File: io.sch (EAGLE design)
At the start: 34 parts, among them J1 SJ-3502-SMT-TR, Q1 MMBT2222A, Q2 2SCR574D3TL1, U1 MCP1703T-5002E, U3 LM386M-1, X1 Antenna

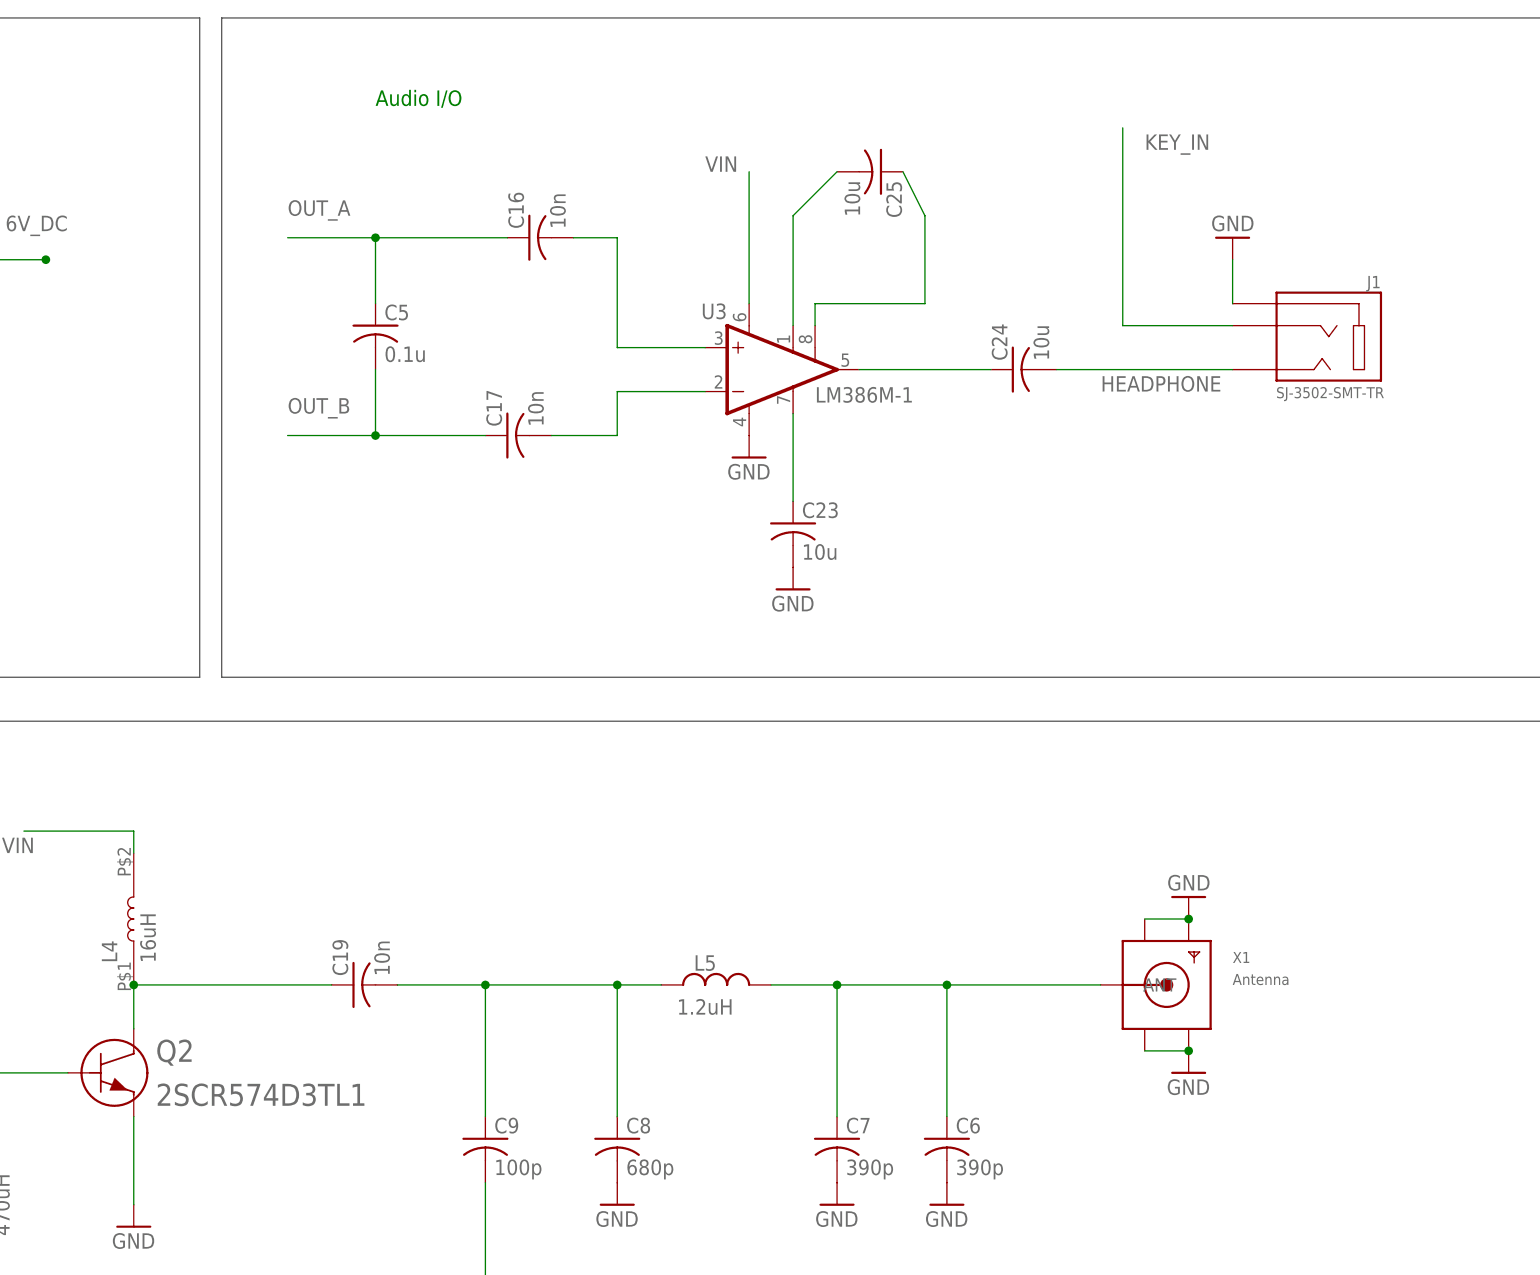
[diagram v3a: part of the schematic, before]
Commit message: Updated boarts to v1.1
9VuTX Version 1.1

Several adjustments after mockup with V 1.0 of the board. That first version would be non-functional due to a few layout mismatches.

* fixed 2nd transistor layout to actually match part / spec (TO-252)
* rotated potentiometers 180 degrees so they face outward instead toward the middle of the board
* expanded pads of L2 (450uH inductor) to match recommended spec
* replaced phone jack with a true surface mount version (SJ-3523-SMT-TR)
* re-arranged the IO board to allow for the different phone jack
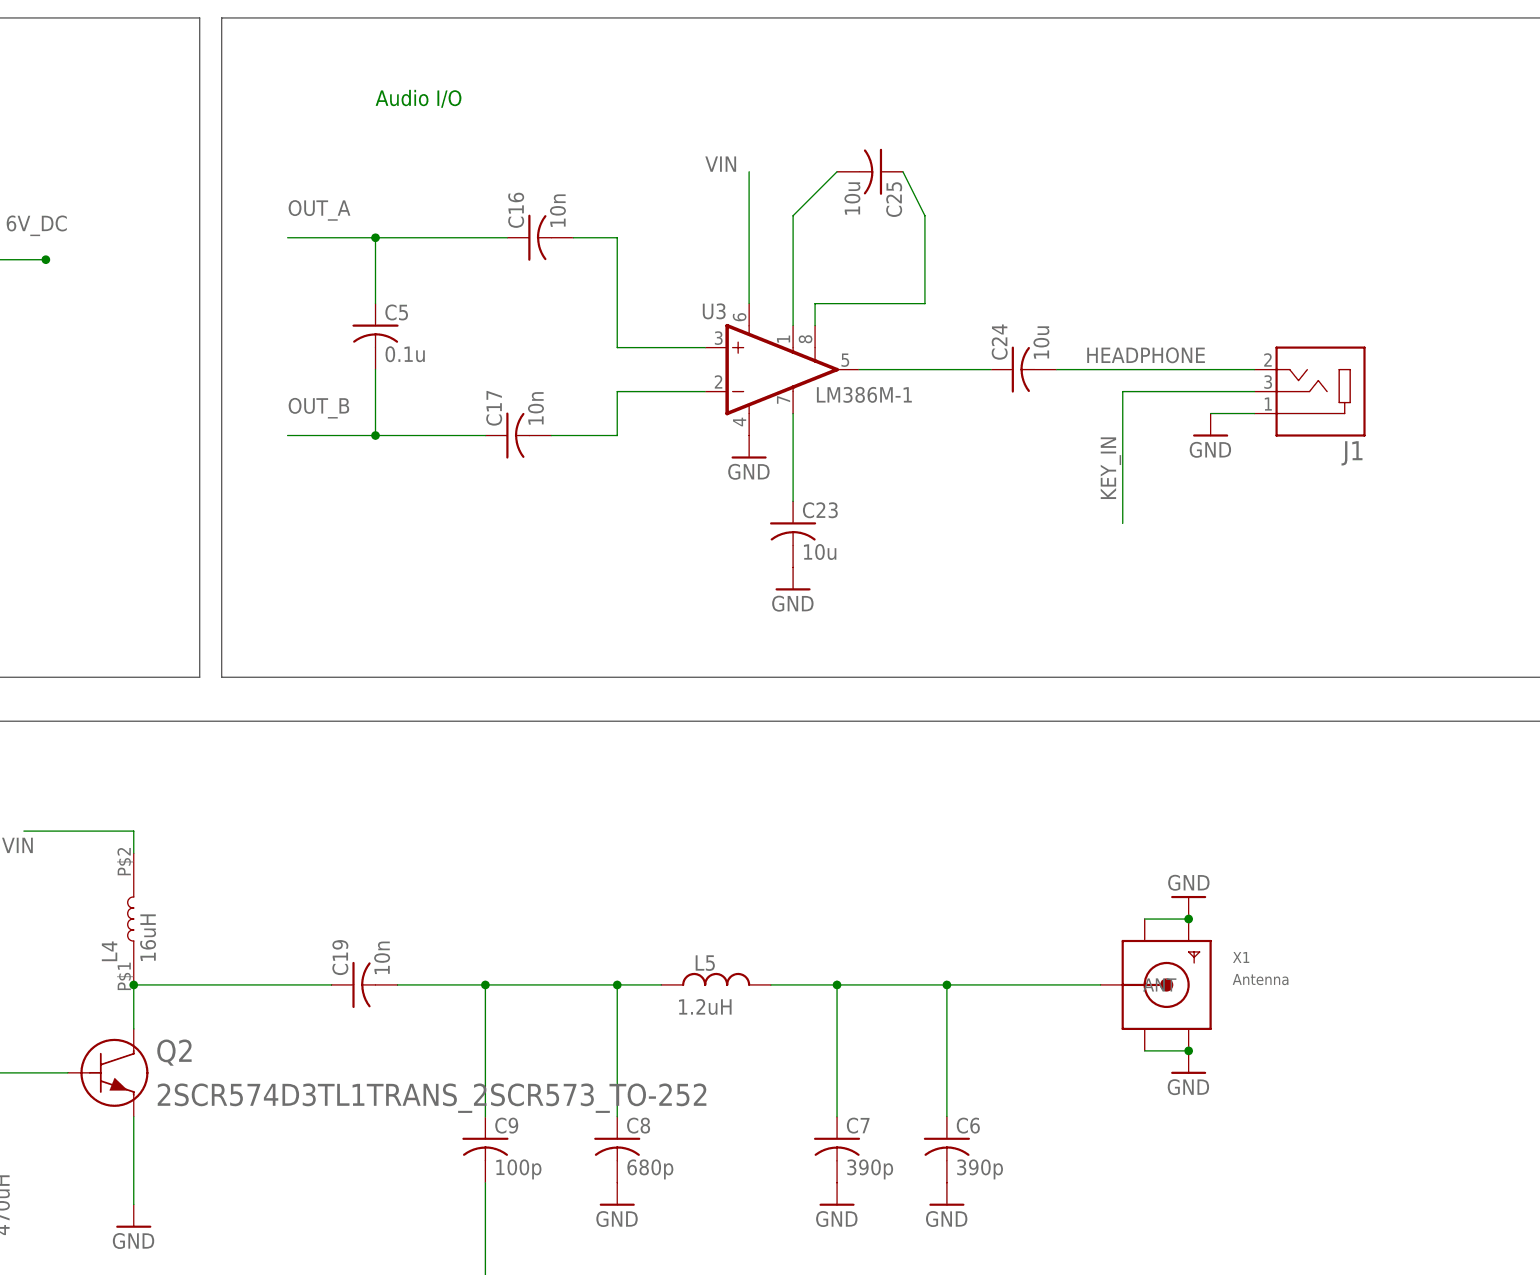
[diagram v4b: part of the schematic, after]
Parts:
- J1: value SJ-3502-SMT-TR -> SJ-3523-SMT-TR; device Audio Connectors:SJ-3502-SMT-TR -> SJ-3523-SMT-TR:SJ-3523-SMT-TR
- L2: device Inductor:L_CHIP-1008(2520-METRIC) -> zort2:L_CHIP-1008(2520-METRIC)
- Q2: value 2SCR574D3TL1 -> 2SCR574D3TL1TRANS_2SCR573_TO-252; device zort2:2SCR574D3TL1 -> zort2:2SCR574D3TL1TRANS_2SCR573_TO-252
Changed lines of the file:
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@@
 <part name="GND8" library="supply1" library_urn="urn:adsk.eagle:library:371" deviceset="GND" device=""/>
 <part name="GND9" library="supply1" library_urn="urn:adsk.eagle:library:371" deviceset="GND" device=""/>
-<part name="J1" library="Audio Connectors" library_urn="urn:adsk.eagle:library:16251796" deviceset="SJ-3502-SMT-TR" device="" package3d_urn="urn:adsk.eagle:package:16225242/5"/>
 <part name="GND10" library="supply1" library_urn="urn:adsk.eagle:library:371" deviceset="GND" device=""/>
 <part name="C12" library="adafruit" library_urn="urn:adsk.eagle:library:420" deviceset="C-US" device="C0805" package3d_urn="urn:adsk.eagle:package:6240337/1" value="150p"/>
@@
 <part name="L5" library="Inductor" library_urn="urn:adsk.eagle:library:16378440" deviceset="L" device="CHIP-0805(2012-METRIC)" package3d_urn="urn:adsk.eagle:package:16378480/1" technology="_" value="1.2uH"/>
 <part name="L4" library="zort2" deviceset="B966AS-160M-P3" device="" value="16uH"/>
-<part name="L2" library="Inductor" library_urn="urn:adsk.eagle:library:16378440" deviceset="L" device="CHIP-1008(2520-METRIC)" package3d_urn="urn:adsk.eagle:package:16378469/1" technology="_" value="470uH"/>
-<part name="Q2" library="zort2" deviceset="2SCR574D3TL1" device=""/>
 <part name="Q1" library="zort2" deviceset="MMBT2222A-7-F" device="SOT-23_DIO-M" value="MMBT2222A"/>
 <part name="U$1" library="zort2" deviceset="9V_968" device="9V_968_SMD"/>
+<part name="Q2" library="zort2" deviceset="2SCR574D3TL1" device="TRANS_2SCR573_TO-252"/>
+<part name="L2" library="zort2" deviceset="L" device="CHIP-1008(2520-METRIC)" package3d_urn="urn:adsk.eagle:package:16378469/1" technology="_" value="470uH"/>
+<part name="J1" library="SJ-3523-SMT-TR" deviceset="SJ-3523-SMT-TR" device=""/>
 </parts>
 <sheets>
@@
 <attribute name="VALUE" x="116.84" y="53.34" size="1.778" layer="96"/>
 </instance>
-<instance part="J1" gate="G$1" x="182.88" y="83.82" smashed="yes" rot="MR0">
-<attribute name="VALUE" x="187.706" y="77.978" size="1.27035" layer="96" rot="MR0"/>
-<attribute name="NAME" x="187.32991875" y="90.68325" size="1.4224" layer="95" rot="MR0"/>
-</instance>
-<instance part="GND10" gate="1" x="170.18" y="96.52" smashed="yes" rot="R180">
-<attribute name="VALUE" x="172.72" y="99.06" size="1.778" layer="96" rot="R180"/>
+<instance part="GND10" gate="1" x="167.64" y="73.66" smashed="yes">
+<attribute name="VALUE" x="165.1" y="71.12" size="1.778" layer="96"/>
 </instance>
 <instance part="C12" gate="G$1" x="-73.66" y="17.78" smashed="yes">
@@
 <attribute name="VALUE" x="45.72271875" y="12.694559375" size="1.779909375" layer="96" rot="R90"/>
 </instance>
+<instance part="Q1" gate="A" x="-60.96" y="-20.32" smashed="yes">
+<attribute name="NAME" x="-50.4444" y="-13.7414" size="2.0828" layer="95" ratio="6" rot="SR0"/>
+<attribute name="VALUE" x="-51.0794" y="-26.4414" size="2.0828" layer="96" ratio="6" rot="SR0"/>
+</instance>
+<instance part="U$1" gate="G$1" x="-78.74" y="88.9" smashed="yes"/>
+<instance part="Q2" gate="A" x="40.64" y="0" smashed="yes">
+<attribute name="NAME" x="45.72" y="1.27" size="2.54" layer="95" ratio="10" rot="SR0"/>
+<attribute name="VALUE" x="45.72" y="-3.81" size="2.54" layer="96" ratio="10" rot="SR0"/>
+</instance>
 <instance part="L2" gate="G$1" x="25.4" y="-15.24" smashed="yes" rot="R90">
 <attribute name="NAME" x="22.86" y="-15.24" size="1.778" layer="95" rot="R90" align="center"/>
 <attribute name="VALUE" x="27.94" y="-15.24" size="1.778" layer="96" rot="R90" align="center"/>
 </instance>
-<instance part="Q2" gate="A" x="40.64" y="0" smashed="yes">
-<attribute name="NAME" x="45.72" y="1.27" size="2.54" layer="95" ratio="10" rot="SR0"/>
-<attribute name="VALUE" x="45.72" y="-3.81" size="2.54" layer="96" ratio="10" rot="SR0"/>
-</instance>
-<instance part="Q1" gate="A" x="-60.96" y="-20.32" smashed="yes">
-<attribute name="NAME" x="-50.4444" y="-13.7414" size="2.0828" layer="95" ratio="6" rot="SR0"/>
-<attribute name="VALUE" x="-51.0794" y="-26.4414" size="2.0828" layer="96" ratio="6" rot="SR0"/>
-</instance>
-<instance part="U$1" gate="G$1" x="-78.74" y="88.9" smashed="yes"/>
+<instance part="J1" gate="G$1" x="180.34" y="78.74" smashed="yes" rot="R180">
+<attribute name="NAME" x="185.440409375" y="73.002040625" size="2.201440625" layer="95" rot="R180"/>
+</instance>
 </instances>
 <busses>
@@
 </segment>
 <segment>
+<pinref part="GND10" gate="1" pin="GND"/>
+<wire x1="167.64" y1="76.2" x2="172.72" y2="76.2" width="0.1524" layer="91"/>
 <pinref part="J1" gate="G$1" pin="1"/>
-<pinref part="GND10" gate="1" pin="GND"/>
-<wire x1="170.18" y1="93.98" x2="170.18" y2="88.9" width="0.1524" layer="91"/>
 </segment>
 <segment>
@@
 </segment>
 <segment>
+<pinref part="GND1" gate="1" pin="GND"/>
+<pinref part="U$1" gate="G$1" pin="P$2"/>
+</segment>
+<segment>
 <pinref part="GND21" gate="1" pin="GND"/>
 <pinref part="L2" gate="G$1" pin="1"/>
-</segment>
-<segment>
-<pinref part="GND1" gate="1" pin="GND"/>
-<pinref part="U$1" gate="G$1" pin="P$2"/>
 </segment>
 </net>
@@
 <segment>
 <pinref part="C24" gate="G$1" pin="2"/>
+<wire x1="149.86" y1="81.28" x2="172.72" y2="81.28" width="0.1524" layer="91"/>
+<label x="153.162" y="82.042" size="1.778" layer="95"/>
 <pinref part="J1" gate="G$1" pin="2"/>
-<wire x1="149.86" y1="81.28" x2="170.18" y2="81.28" width="0.1524" layer="91"/>
-<label x="154.94" y="78.74" size="1.778" layer="95"/>
 </segment>
 </net>
 <net name="KEY_IN" class="0">
 <segment>
+<label x="154.94" y="73.66" size="1.778" layer="95" rot="R270"/>
 <pinref part="J1" gate="G$1" pin="3"/>
-<wire x1="170.18" y1="86.36" x2="157.48" y2="86.36" width="0.1524" layer="91"/>
-<wire x1="157.48" y1="86.36" x2="157.48" y2="109.22" width="0.1524" layer="91"/>
-<label x="160.02" y="106.68" size="1.778" layer="95"/>
+<wire x1="172.72" y1="78.74" x2="157.48" y2="78.74" width="0.1524" layer="91"/>
+<wire x1="157.48" y1="78.74" x2="157.48" y2="63.5" width="0.1524" layer="91"/>
 </segment>
 <segment>
@@
 </segment>
 </net>
-<net name="N$23" class="0">
+<net name="N$23" class="1">
 <segment>
 <pinref part="R7" gate="G$1" pin="2"/>
@@
 <wire x1="25.4" y1="0" x2="35.56" y2="0" width="0.1524" layer="91"/>
 <junction x="25.4" y="0"/>
+<pinref part="Q2" gate="A" pin="1"/>
 <pinref part="L2" gate="G$1" pin="2"/>
-<pinref part="Q2" gate="A" pin="1"/>
-</segment>
-</net>
-<net name="N$24" class="0">
+</segment>
+</net>
+<net name="N$24" class="1">
 <segment>
 <wire x1="43.18" y1="5.08" x2="43.18" y2="10.16" width="0.1524" layer="91"/>
@@
 </segment>
 </net>
-<net name="N$25" class="0">
+<net name="N$25" class="1">
 <segment>
 <pinref part="C19" gate="G$1" pin="2"/>
@@
 </segment>
 </net>
-<net name="N$26" class="0">
+<net name="N$26" class="1">
 <segment>
 <wire x1="116.84" y1="10.16" x2="124.46" y2="10.16" width="0.1524" layer="91"/>

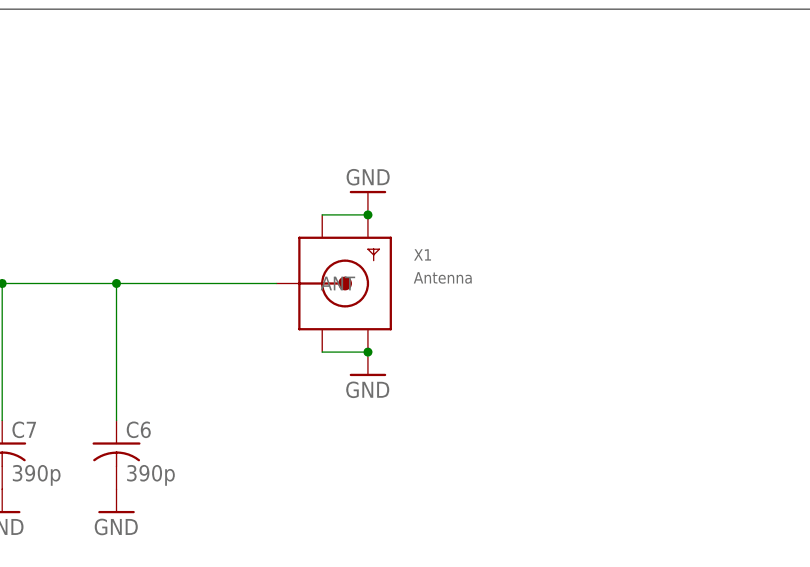
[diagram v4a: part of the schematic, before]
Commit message: continuing on v 1.1
* removed "label" label from SMA connector
* increased the width of some lines likely to carry higher current
* attempted to clean up some little stuff
* updated images
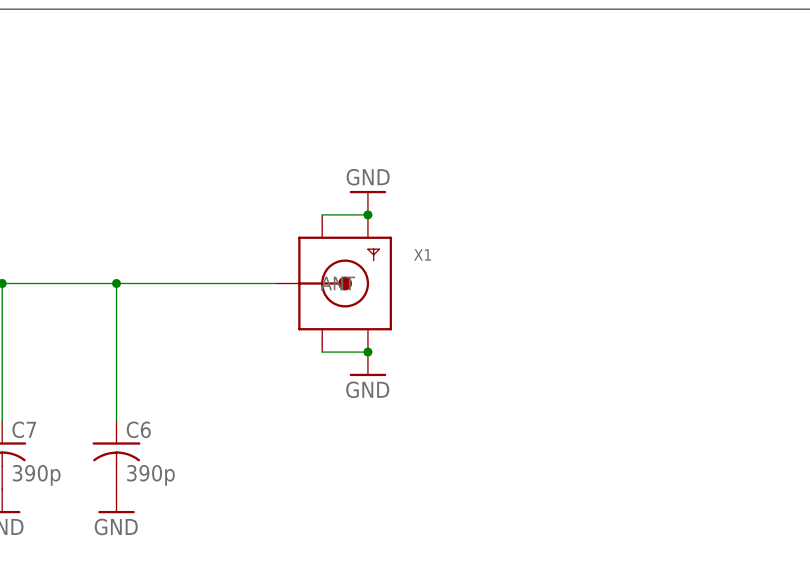
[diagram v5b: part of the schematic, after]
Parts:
- X1: value Antenna -> (none); device adafruit:SMACONNECTOR_EDGE -> zort2:SMACONNECTOR_EDGE
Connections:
- new net N$1: X1.GND3
- new net N$2: X1.GND1
- net GND: no longer X1.GND1, X1.GND3
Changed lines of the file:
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@@
 <part name="GND19" library="supply1" library_urn="urn:adsk.eagle:library:371" deviceset="GND" device=""/>
 <part name="GND20" library="supply1" library_urn="urn:adsk.eagle:library:371" deviceset="GND" device=""/>
-<part name="X1" library="adafruit" library_urn="urn:adsk.eagle:library:420" deviceset="SMACONNECTOR" device="_EDGE" package3d_urn="urn:adsk.eagle:package:6240945/1" value="Antenna"/>
 <part name="L3" library="MLF2012E5R6KT000" deviceset="MLF2012E5R6KT000" device="" value="5.6uH"/>
 <part name="R7" library="adafruit" library_urn="urn:adsk.eagle:library:420" deviceset="R-US_" device="M0805" package3d_urn="urn:adsk.eagle:package:6240587/1" value="100"/>
@@
 <part name="L2" library="zort2" deviceset="L" device="CHIP-1008(2520-METRIC)" package3d_urn="urn:adsk.eagle:package:16378469/1" technology="_" value="470uH"/>
 <part name="J1" library="SJ-3523-SMT-TR" deviceset="SJ-3523-SMT-TR" device=""/>
+<part name="X1" library="zort2" deviceset="SMACONNECTOR" device="_EDGE" package3d_urn="urn:adsk.eagle:package:6240945/1"/>
 </parts>
 <sheets>
@@
 <attribute name="VALUE" x="134.62" y="-17.78" size="1.778" layer="96"/>
 </instance>
-<instance part="X1" gate="G$1" x="162.56" y="10.16" smashed="yes">
-<attribute name="NAME" x="170.18" y="12.7" size="1.27" layer="95"/>
-<attribute name="VALUE" x="170.18" y="10.16" size="1.27" layer="95"/>
-</instance>
 <instance part="L3" gate="G$1" x="-17.78" y="7.62" smashed="yes" rot="R90">
 <attribute name="NAME" x="-19.68818125" y="2.53153125" size="1.780959375" layer="95" rot="R90"/>
@@
 <instance part="J1" gate="G$1" x="180.34" y="78.74" smashed="yes" rot="R180">
 <attribute name="NAME" x="185.440409375" y="73.002040625" size="2.201440625" layer="95" rot="R180"/>
+</instance>
+<instance part="X1" gate="G$1" x="162.56" y="10.16" smashed="yes">
+<attribute name="NAME" x="170.18" y="12.7" size="1.27" layer="95"/>
+<attribute name="VALUE" x="170.18" y="10.16" size="1.27" layer="95"/>
 </instance>
 </instances>
@@
 </segment>
 <segment>
+<pinref part="GND23" gate="1" pin="GND"/>
 <pinref part="X1" gate="G$1" pin="GND4"/>
-<pinref part="GND23" gate="1" pin="GND"/>
-<pinref part="X1" gate="G$1" pin="GND3"/>
-<wire x1="160.02" y1="2.54" x2="165.1" y2="2.54" width="0.1524" layer="91"/>
 <junction x="165.1" y="2.54"/>
 </segment>
 <segment>
-<pinref part="X1" gate="G$1" pin="GND1"/>
+<pinref part="GND24" gate="1" pin="GND"/>
 <pinref part="X1" gate="G$1" pin="GND2"/>
-<wire x1="160.02" y1="17.78" x2="165.1" y2="17.78" width="0.1524" layer="91"/>
-<pinref part="GND24" gate="1" pin="GND"/>
 <junction x="165.1" y="17.78"/>
 </segment>
@@
 </segment>
 </net>
-<net name="6V_DC" class="0">
+<net name="6V_DC" class="1">
 <segment>
 <wire x1="10.16" y1="93.98" x2="17.78" y2="93.98" width="0.1524" layer="91"/>
@@
 <wire x1="137.16" y1="10.16" x2="124.46" y2="10.16" width="0.1524" layer="91"/>
 <junction x="124.46" y="10.16"/>
-<pinref part="X1" gate="G$1" pin="ANT"/>
 <wire x1="154.94" y1="10.16" x2="137.16" y2="10.16" width="0.1524" layer="91"/>
 <junction x="137.16" y="10.16"/>
 <pinref part="L5" gate="G$1" pin="2"/>
-</segment>
-</net>
+<pinref part="X1" gate="G$1" pin="ANT"/>
+</segment>
+</net>
+<net name="N$1" class="0">
+<segment>
+<wire x1="160.02" y1="2.54" x2="165.0238" y2="2.54" width="0.1524" layer="91"/>
+<pinref part="X1" gate="G$1" pin="GND3"/>
+</segment>
+</net>
+<net name="N$2" class="0">
+<segment>
+<wire x1="160.02" y1="17.78" x2="165.0238" y2="17.78" width="0.1524" layer="91"/>
+<pinref part="X1" gate="G$1" pin="GND1"/>
+</segment>
+</net>
